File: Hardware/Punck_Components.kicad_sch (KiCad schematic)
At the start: 150 parts, among them J1 Conn_01x08_Male, J2 Conn_01x08_Male, J3 Conn_01x08_Male, J4 Conn_01x08_Male, J5 SWD_Header, J6 USB_B_Micro, J7 Eurorack_10_pin_power, J8 I2C_TestPoint, U1 MCP6004, U10 LD1117-3.3-4Tab, U2 TL074, U3 MCP6004, U4 IS42S16800F-7TLI, U5 STM32H743ZITx, U6 TL072, U7 AS3364, U8 PCM5100APW, U9 LM2675M-5, Y1 8MHz 20pF

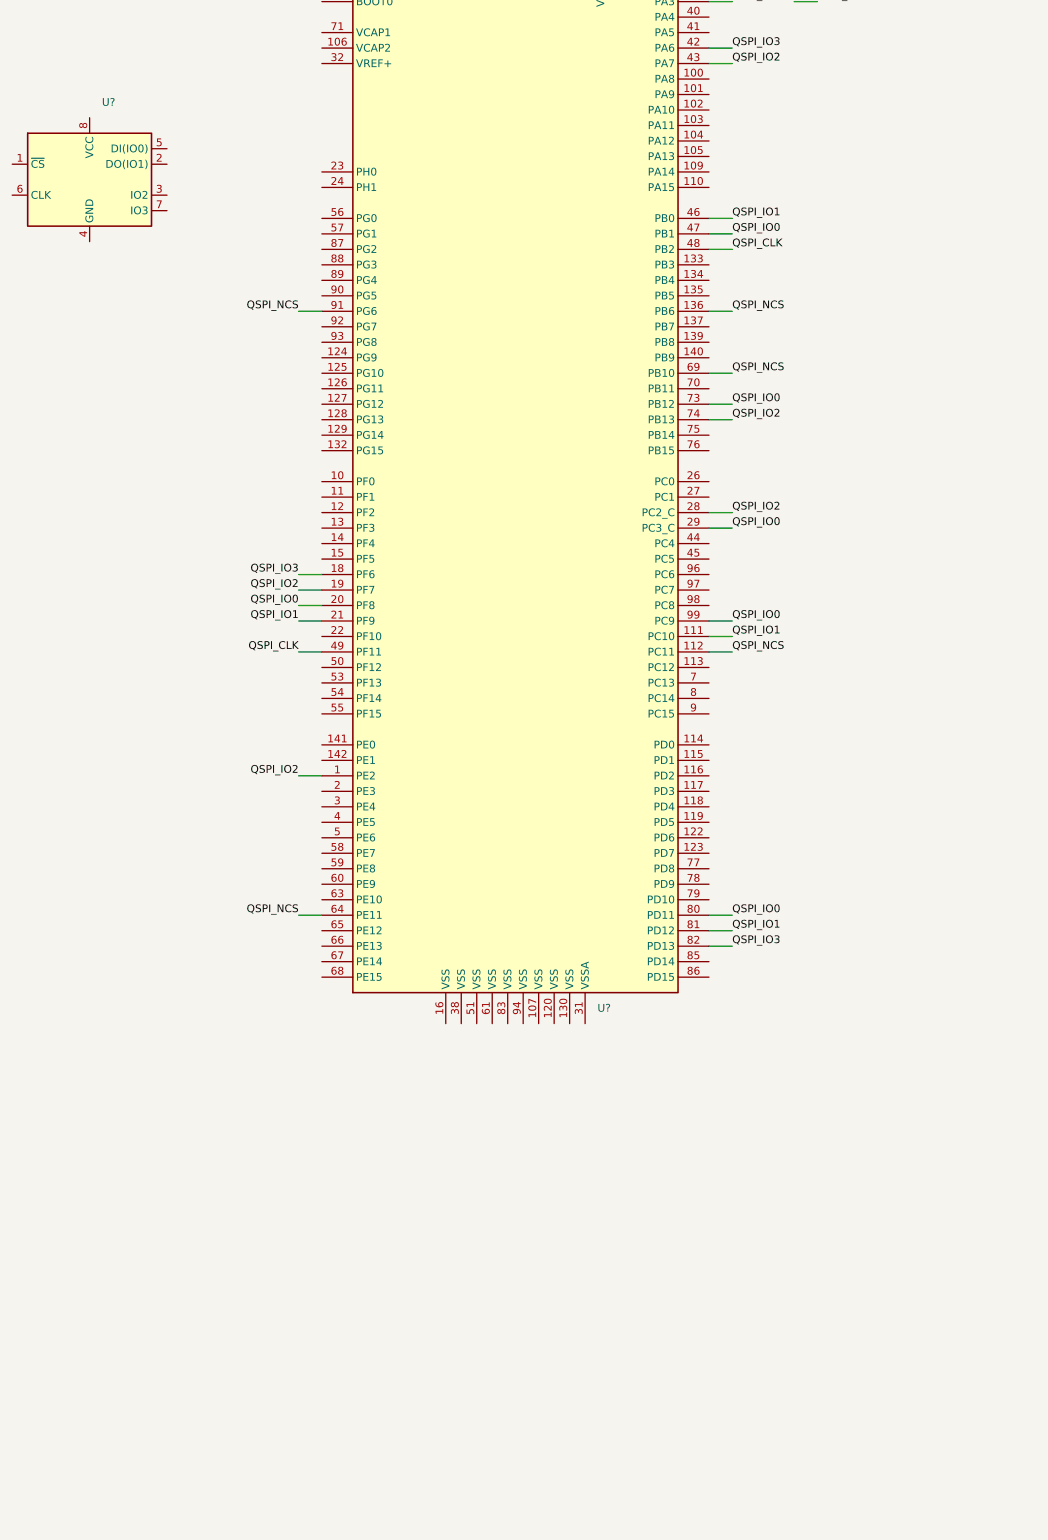
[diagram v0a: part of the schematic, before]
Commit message: Serial MIDI working
Fixed issues allowing A/B samples to be played simultaneously
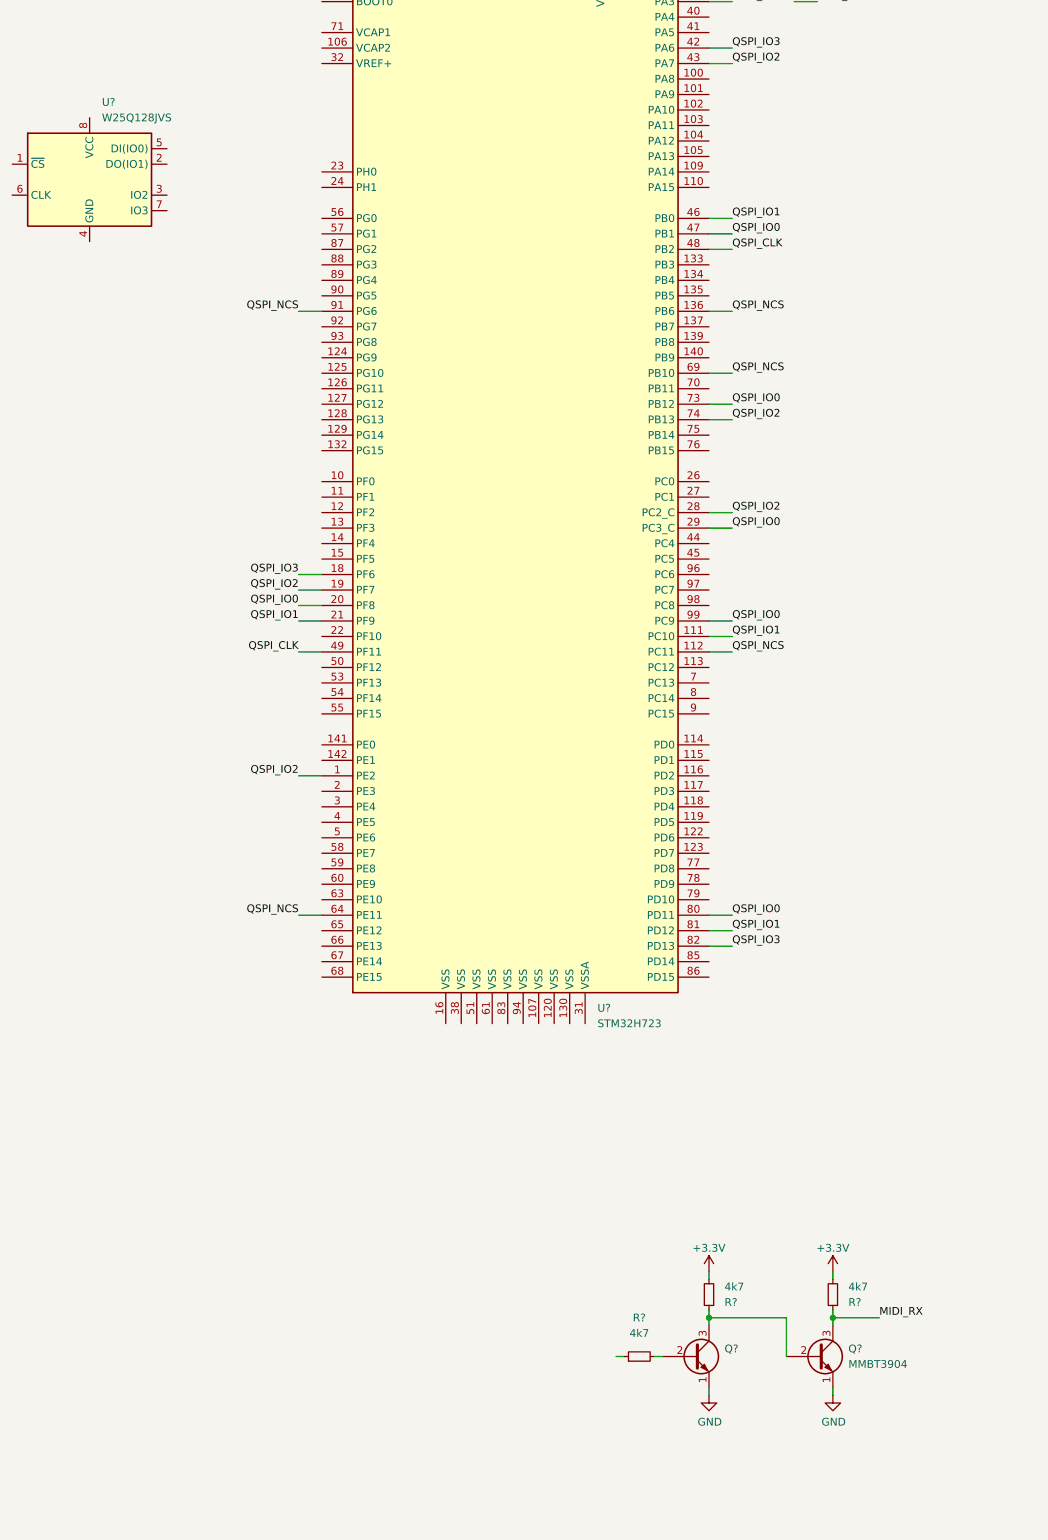
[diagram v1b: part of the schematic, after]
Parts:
- added Q?: (no value), Package_TO_SOT_THT:TO-92_Inline, symbol Transistor_BJT:2N3904
- added Q?: MMBT3904, Package_TO_SOT_THT:TO-92_Inline, symbol Transistor_BJT:2N3904
- added R? (x3): 4k7, Resistor_SMD:R_0603_1608Metric, symbol Device:R_Small
- U?: value (none) -> STM32H723; footprint (none) -> Package_QFP:LQFP-144_20x20mm_P0.5mm
- U?: value (none) -> W25Q128JVS; footprint (none) -> Package_SO:SOIC-8_5.23x5.23mm_P1.27mm
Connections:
- net +3V3: now also R?.2, R?.2
- net GND: now also Q?.1 (E), Q?.1 (E)
- new net: Q?.2 (B), Q?.3 (C), R?.1
- new net: Q?.2 (B), R?.2
- new net MIDI_RX: Q?.3 (C), R?.1

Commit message: STarted PCB layout; ADC control updates
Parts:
- removed C15, C16, C17, C18, C19, C20, C21: 100nF, Capacitors_SMD:C_0603_HandSoldering, symbol Device:C_Small
- removed C49, C50, C51, C52: 560pF, Capacitors_SMD:C_0603_HandSoldering, symbol Device:C_Small
- removed C56: 10nF, Capacitors_SMD:C_0603_HandSoldering, symbol Device:C_Small
- removed J8: I2C_TestPoint, Pin_Headers:Pin_Header_Straight_1x02_Pitch2.54mm, symbol Connector:Conn_01x02_Female
- removed Q?: MMBT3904, Package_TO_SOT_THT:TO-92_Inline, symbol Transistor_BJT:2N3904
- removed R37, R38, R39, R40: 30k, Resistors_SMD:R_0603_HandSoldering, symbol Device:R_Small
- removed R41, R42, R43, R44: 510R, Resistors_SMD:R_0603_HandSoldering, symbol Device:R_Small
- removed R45: 100R, Resistors_SMD:R_0603_HandSoldering, symbol Device:R_Small
- removed R?: 4k7, Resistor_SMD:R_0603_1608Metric, symbol Device:R_Small
- removed U4: IS42S16800F-7TLI, Custom_Footprints:TSOP-II-54_22.2x10.16mm_P0.8mm, symbol SDRAM:IS42S16160
- removed U7: AS3364, Housings_SOIC:SOIC-16_3.9x9.9mm_Pitch1.27mm, symbol Audio:SSI2164
- removed U?: STM32H723, Package_QFP:LQFP-144_20x20mm_P0.5mm, symbol STM32H7:STM32H723
- Q1: renamed from Q?; value (none) -> MMBT3904
- gave numbers to parts that had none: 3
- renumbered R46 to R48, TP13 to TP10, TP10 to TP11, TP11 to TP12, TP12 to TP13, U3 to U1, U8 to U10, U9 to U11, U10 to U12, U1 to U3, U5 to U6, U6 to U7
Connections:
- net FMC_~{BL0} is gone; now on net MIDI_RX: U6.141 (PE0)
- net +3V3: now also U5.8 (VCC)
- net AUDIO_IN_L: no longer U6.37 (PA3)
- net AUDIO_IN_R: no longer U6.36 (PA2)
- net CHORUS: no longer U6.125 (PG10)
- net CLOCK_SCALED: no longer U6.48 (PB2)
- net DELAY_CV_SCALED_L: no longer U6.42 (PA6)
- net DELAY_CV_SCALED_R: no longer U6.34 (PA0)
- net DELAY_POT_L: no longer U6.47 (PB1)
- net DELAY_POT_R: no longer U6.35 (PA1)
- net FEEDBACK_CV_SCALED: no longer U6.43 (PA7)
- net FEEDBACK_POT: no longer U6.46 (PB0)
- net FILTER_CV_SCALED: no longer U6.44 (PC4)
- net GND: now also U5.4 (GND)
- net HP_MODE: no longer U6.112 (PC11)
- net LED_SPI_CLK: no longer U6.128 (PG13)
- net LED_SPI_DATA: no longer U6.129 (PG14)
- net LOCK_BTN: no longer U6.134 (PB4)
- net LP_MODE: no longer U6.111 (PC10)
- net MIDI_RX: now also Q1.3 (C), R46.1
- net MODE1: no longer U6.1 (PE2)
- net MODE2: no longer U6.2 (PE3)
- net QSPI_CLK: now also U5.6 (CLK), U6.48 (PB2)
- net QSPI_IO0: now also U5.5 (DI(IO0)), U6.80 (PD11)
- net QSPI_IO1: now also U5.2 (DO(IO1)), U6.81 (PD12)
- net QSPI_IO2: now also U5.3 (IO2), U6.1 (PE2)
- net QSPI_IO3: now also U5.7 (IO3), U6.82 (PD13)
- net QSPI_NCS: now also U5.1 (~{CS}), U6.91 (PG6)
- net STEREO_WIDE: no longer U6.113 (PC12)
- net TONE_POT: no longer U6.27 (PC1)
- net WET_DRY_MIX: no longer U6.45 (PC5)
- net MIDI_IN: now reaches R49.1
- net FMC_A0: no longer names the net of U6.10 (PF0)
- net FMC_A1: no longer names the net of U6.11 (PF1)
- net FMC_A10: no longer names the net of U6.56 (PG0)
- net FMC_A11: no longer names the net of U6.57 (PG1)
- net FMC_A12: no longer names the net of U6.87 (PG2)
- net FMC_A2: no longer names the net of U6.12 (PF2)
- net FMC_A3: no longer names the net of U6.13 (PF3)
- net FMC_A4: no longer names the net of U6.14 (PF4)
- net FMC_A5: no longer names the net of U6.15 (PF5)
- net FMC_A6: no longer names the net of U6.50 (PF12)
- net FMC_A7: no longer names the net of U6.53 (PF13)
- net FMC_A8: no longer names the net of U6.54 (PF14)
- net FMC_A9: no longer names the net of U6.55 (PF15)
- net FMC_BA0: no longer names the net of U6.89 (PG4)
- net FMC_BA1: no longer names the net of U6.90 (PG5)
- net FMC_D0: no longer names the net of U6.85 (PD14)
- net FMC_D1: no longer names the net of U6.86 (PD15)
- net FMC_D10: no longer names the net of U6.66 (PE13)
- net FMC_D11: no longer names the net of U6.67 (PE14)
- net FMC_D12: no longer names the net of U6.68 (PE15)
- net FMC_D13: no longer names the net of U6.77 (PD8)
- net FMC_D14: no longer names the net of U6.78 (PD9)
- net FMC_D15: no longer names the net of U6.79 (PD10)
- net FMC_D2: no longer names the net of U6.114 (PD0)
- net FMC_D3: no longer names the net of U6.115 (PD1)
- net FMC_D4: no longer names the net of U6.58 (PE7)
- net FMC_D5: no longer names the net of U6.59 (PE8)
- net FMC_D6: no longer names the net of U6.60 (PE9)
- net FMC_D7: no longer names the net of U6.63 (PE10)
- net FMC_D8: no longer names the net of U6.64 (PE11)
- net FMC_D9: no longer names the net of U6.65 (PE12)
- net FMC_SDCKE1: no longer names the net of U6.135 (PB5)
- net FMC_SDCLK: no longer names the net of U6.93 (PG8)
- net FMC_SD~{E1}: no longer names the net of U6.136 (PB6)
- net FMC_SD~{WE}: no longer names the net of U6.26 (PC0)
- net FMC_~{BL1}: no longer names the net of U6.142 (PE1)
- net FMC_~{CAS}: no longer names the net of U6.132 (PG15)
- net FMC_~{RAS}: no longer names the net of U6.49 (PF11)
- net I2C1_SCL: no longer names the net of U6.139 (PB8)
- net I2C1_SDA: no longer names the net of U6.137 (PB7)
- net MIX_DRY_CTL renamed DAC1
- net MIX_WET_CTL renamed DAC2
- no-connect marks 43 -> 39
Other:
- note removed: "AS3364D (linear VCA) with R43 and C56 in place; Remove for SSI2164 (exponential)"
- note removed: "DRAM"
- moved on the sheet: Q1, R46, R49, U5
